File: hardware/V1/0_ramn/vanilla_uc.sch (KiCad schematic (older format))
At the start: 14 parts, among them J4 , U4 ATA6561-GAQW-N, U5 STM32L443CCTx, Y2 NX3225GD-8MHZ-STD-CRA-3

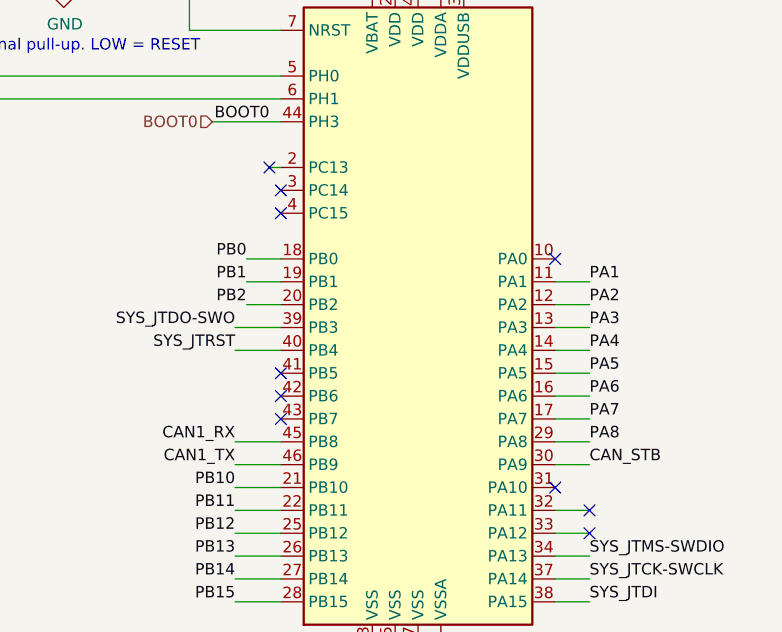
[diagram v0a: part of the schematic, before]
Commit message: Added initial V1 Firmware and Scripts
- Minor hardware fixes
- Minor documentation fixes
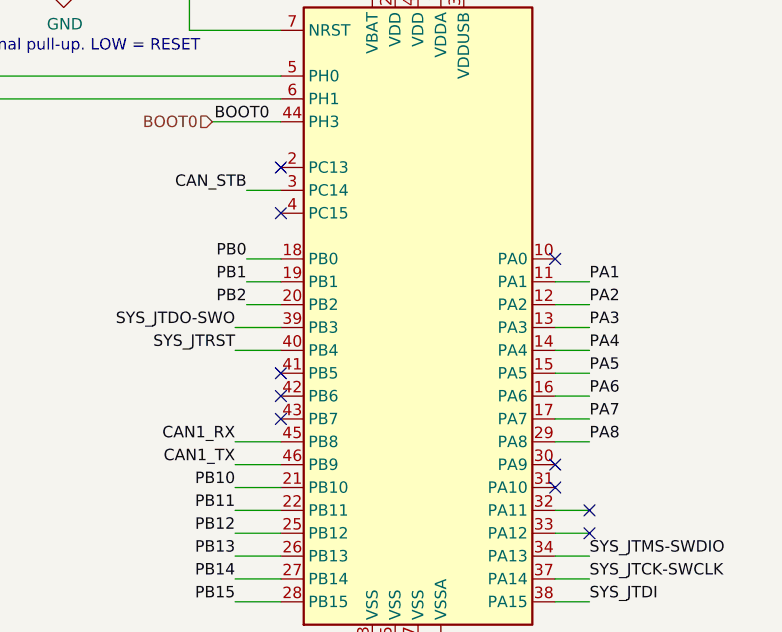
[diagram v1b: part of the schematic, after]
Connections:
- net CAN_STB: now also U5.3 (PC14); no longer U5.30 (PA9)
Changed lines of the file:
@@
 Sheet 4 9
 Title "RAMN: Resistant Automotive Miniature Network V1.0"
-Date "2021-02-20"
-Rev "A"
+Date "2021-06-01"
+Rev "B2L"
 Comp "Copyright (c) 2021 TOYOTA MOTOR CORPORATION. ALL RIGHTS RESERVED."
 Comment1 ""
@@
 BOOT0
 Wire Wire Line
-	8600 3550 8550 3550
-Text Label 9950 4850 0    50   ~ 0
-CAN_STB
-Wire Wire Line
 	8400 4750 8600 4750
 Text Label 8400 4750 2    50   ~ 0
@@
 Wire Wire Line
 	6550 3250 6550 3350
-NoConn ~ 8600 3650
 NoConn ~ 8600 3750
 $Sheet
@@
 Text Label 8200 2700 0    50   ~ 0
 nRST
-NoConn ~ 8550 3550
 NoConn ~ 9800 4950
 NoConn ~ 9800 3950
@@
 BOOT0
 Wire Wire Line
-	9950 4850 9800 4850
-Wire Wire Line
 	3050 3150 3050 3100
 Connection ~ 3050 3100
@@
 	1    0    0    -1
 $EndComp
+Text Label 8450 3650 2    50   ~ 0
+CAN_STB
+NoConn ~ 8600 3550
+Wire Wire Line
+	8600 3650 8450 3650
+NoConn ~ 9800 4850
 $EndSCHEMATC

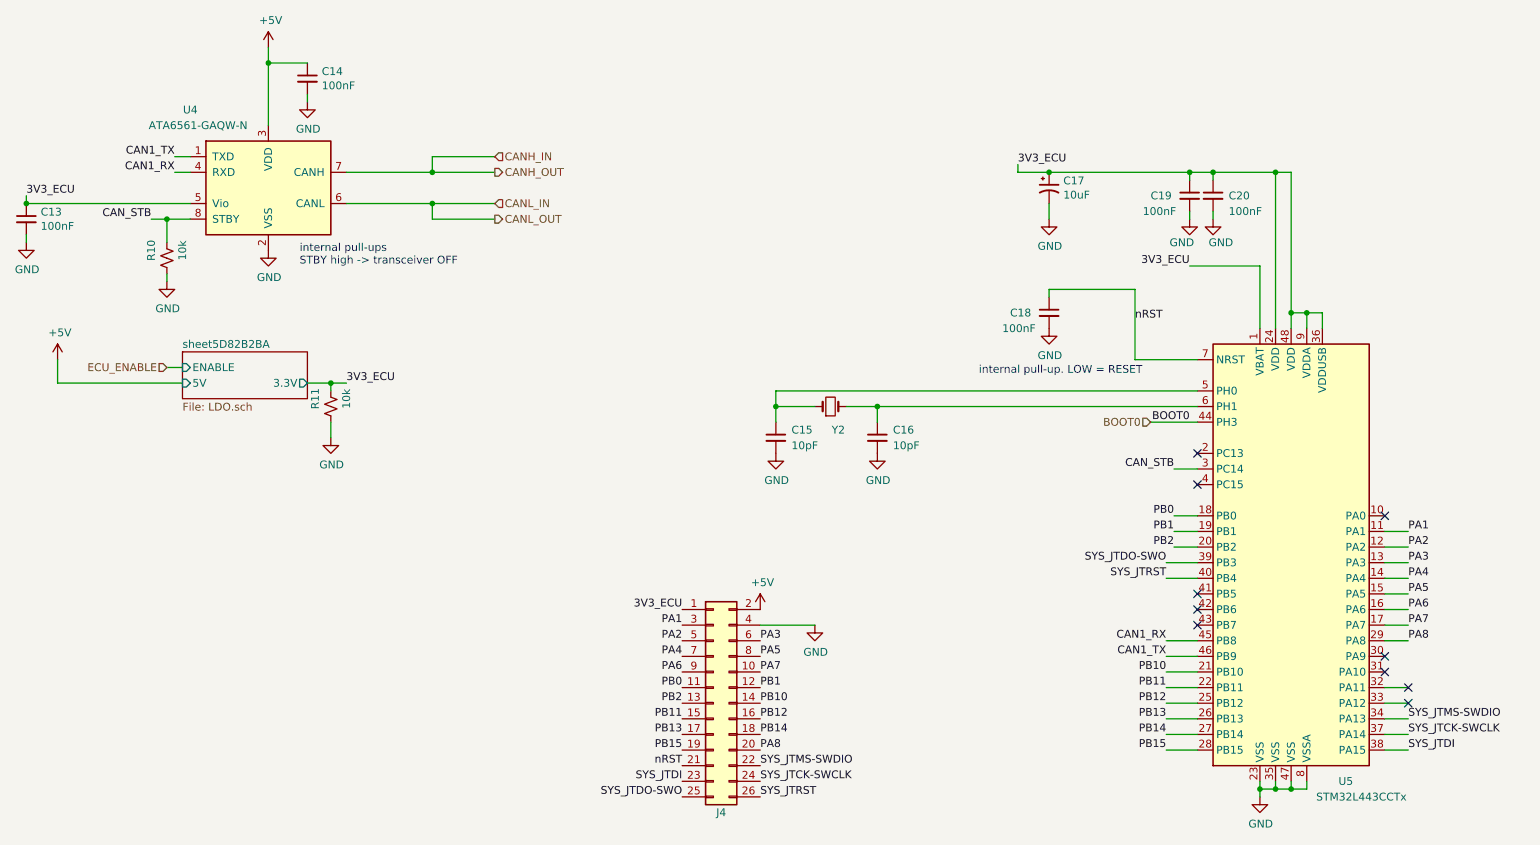
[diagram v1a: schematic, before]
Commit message: Updated schematics to show BOOT0 resistor settings for STM32L5 microcontrollers
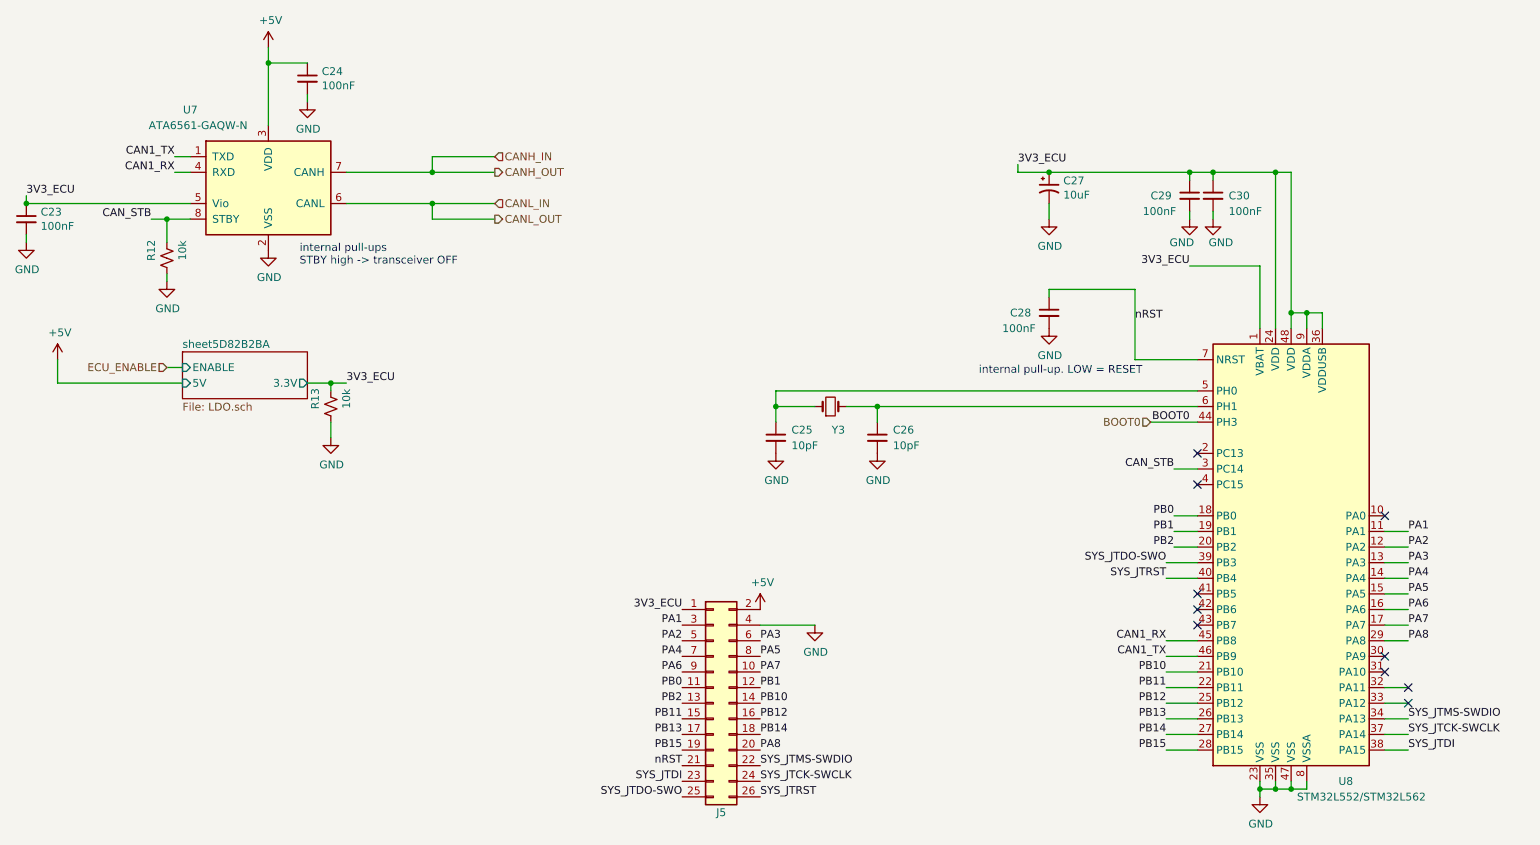
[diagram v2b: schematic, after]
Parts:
- U5: value STM32L443CCTx -> STM32L552/STM32L562
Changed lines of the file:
@@
 $Descr A4 11693 8268
 encoding utf-8
-Sheet 4 9
+Sheet 6 9
 Title "RAMN: Resistant Automotive Miniature Network V1.0"
-Date "2021-06-01"
+Date "2024-02-20"
 Rev "B2L"
-Comp "Copyright (c) 2021 TOYOTA MOTOR CORPORATION. ALL RIGHTS RESERVED."
+Comp "Copyright (c) 2024 TOYOTA MOTOR CORPORATION. ALL RIGHTS RESERVED."
 Comment1 ""
 Comment2 ""
@@
 AR Path="/5D815E09/5D82B2DA" Ref="#PWR028"  Part="1"
 AR Path="/5D8EDE42/5D82B2DA" Ref="#PWR047"  Part="1"
-F 0 "#PWR028" H 2650 2000 50  0001 C CNN
+F 0 "#PWR047" H 2650 2000 50  0001 C CNN
 F 1 "GND" H 2655 2077 50  0000 C CNN
 F 2 "" H 2650 2250 50  0001 C CNN
@@
 AR Path="/5D815E09/5D82B2F8" Ref="#PWR027"  Part="1"
 AR Path="/5D8EDE42/5D82B2F8" Ref="#PWR046"  Part="1"
-F 0 "#PWR027" H 2650 800 50  0001 C CNN
+F 0 "#PWR046" H 2650 800 50  0001 C CNN
 F 1 "+5V" H 2665 1123 50  0000 C CNN
 F 2 "" H 2650 950 50  0001 C CNN
@@
 AR Path="/5D815E09/5D82B303" Ref="#PWR029"  Part="1"
 AR Path="/5D8EDE42/5D82B303" Ref="#PWR048"  Part="1"
-F 0 "#PWR029" H 2900 1050 50  0001 C CNN
+F 0 "#PWR048" H 2900 1050 50  0001 C CNN
 F 1 "GND" H 2905 1127 50  0000 C CNN
 F 2 "" H 2900 1300 50  0001 C CNN
@@
 AR Path="/5D815E09/5D82B30A" Ref="C14"  Part="1"
 AR Path="/5D8EDE42/5D82B30A" Ref="C24"  Part="1"
-F 0 "C14" H 2992 1196 50  0000 L CNN
+F 0 "C24" H 2992 1196 50  0000 L CNN
 F 1 "100nF" H 2992 1105 50  0000 L CNN
 F 2 "Capacitor_SMD:C_0603_1608Metric" H 2900 1150 50  0001 C CNN
@@
 AR Path="/5D815E09/5D82B311" Ref="#PWR024"  Part="1"
 AR Path="/5D8EDE42/5D82B311" Ref="#PWR043"  Part="1"
-F 0 "#PWR024" H 1100 1950 50  0001 C CNN
+F 0 "#PWR043" H 1100 1950 50  0001 C CNN
 F 1 "GND" H 1105 2027 50  0000 C CNN
 F 2 "" H 1100 2200 50  0001 C CNN
@@
 AR Path="/5D815E09/5D82B318" Ref="C13"  Part="1"
 AR Path="/5D8EDE42/5D82B318" Ref="C23"  Part="1"
-F 0 "C13" H 1192 2096 50  0000 L CNN
+F 0 "C23" H 1192 2096 50  0000 L CNN
 F 1 "100nF" H 1192 2005 50  0000 L CNN
 F 2 "Capacitor_SMD:C_0603_1608Metric" H 1100 2050 50  0001 C CNN
@@
 AR Path="/5D815E09/5D82B31E" Ref="U4"  Part="1"
 AR Path="/5D8EDE42/5D82B31E" Ref="U7"  Part="1"
-F 0 "U4" H 2150 2350 50  0000 C CNN
+F 0 "U7" H 2150 2350 50  0000 C CNN
 F 1 "ATA6561-GAQW-N" H 2200 2250 50  0000 C CNN
 F 2 "Package_SO:SOIC-8_3.9x4.9mm_P1.27mm" H 2650 1350 50  0001 C CIN
@@
 AR Path="/5D815E09/5D82B368" Ref="#PWR032"  Part="1"
 AR Path="/5D8EDE42/5D82B368" Ref="#PWR051"  Part="1"
-F 0 "#PWR032" H 5900 3300 50  0001 C CNN
+F 0 "#PWR051" H 5900 3300 50  0001 C CNN
 F 1 "GND" H 5905 3377 50  0000 C CNN
 F 2 "" H 5900 3550 50  0001 C CNN
@@
 AR Path="/5D815E09/5D82B36E" Ref="#PWR034"  Part="1"
 AR Path="/5D8EDE42/5D82B36E" Ref="#PWR053"  Part="1"
-F 0 "#PWR034" H 6550 3300 50  0001 C CNN
+F 0 "#PWR053" H 6550 3300 50  0001 C CNN
 F 1 "GND" H 6555 3377 50  0000 C CNN
 F 2 "" H 6550 3550 50  0001 C CNN
@@
 AR Path="/5D815E09/5D82B376" Ref="C16"  Part="1"
 AR Path="/5D8EDE42/5D82B376" Ref="C26"  Part="1"
-F 0 "C16" H 6650 3500 50  0000 L CNN
+F 0 "C26" H 6650 3500 50  0000 L CNN
 F 1 "10pF" H 6650 3400 50  0000 L CNN
 F 2 "Capacitor_SMD:C_0603_1608Metric" H 6550 3450 50  0001 C CNN
@@
 AR Path="/5D815E09/5D82B37D" Ref="C15"  Part="1"
 AR Path="/5D8EDE42/5D82B37D" Ref="C25"  Part="1"
-F 0 "C15" H 6000 3500 50  0000 L CNN
+F 0 "C25" H 6000 3500 50  0000 L CNN
 F 1 "10pF" H 6000 3400 50  0000 L CNN
 F 2 "Capacitor_SMD:C_0603_1608Metric" H 5900 3450 50  0001 C CNN
@@
 AR Path="/5D815E09/5D82B383" Ref="Y2"  Part="1"
 AR Path="/5D8EDE42/5D82B383" Ref="Y3"  Part="1"
-F 0 "Y2" H 6300 3100 50  0000 C CNN
+F 0 "Y3" H 6300 3100 50  0000 C CNN
 F 1 "NX3225GD-8MHZ-STD-CRA-3" H 6500 3400 50  0001 C CNN
 F 2 "digikey-footprints:SMD-2_3.2x2.5mm" H 6250 3250 50  0001 C CNN
@@
 AR Path="/5D815E09/5D82B396" Ref="#PWR039"  Part="1"
 AR Path="/5D8EDE42/5D82B396" Ref="#PWR058"  Part="1"
-F 0 "#PWR039" H 9000 5500 50  0001 C CNN
+F 0 "#PWR058" H 9000 5500 50  0001 C CNN
 F 1 "GND" H 9005 5577 50  0000 C CNN
 F 2 "" H 9000 5750 50  0001 C CNN
@@
 AR Path="/5D815E09/5D82B3A9" Ref="#PWR036"  Part="1"
 AR Path="/5D8EDE42/5D82B3A9" Ref="#PWR055"  Part="1"
-F 0 "#PWR036" H 7650 2500 50  0001 C CNN
+F 0 "#PWR055" H 7650 2500 50  0001 C CNN
 F 1 "GND" H 7655 2577 50  0000 C CNN
 F 2 "" H 7650 2750 50  0001 C CNN
@@
 AR Path="/5D815E09/5D82B3B0" Ref="C18"  Part="1"
 AR Path="/5D8EDE42/5D82B3B0" Ref="C28"  Part="1"
-F 0 "C18" H 7400 2650 50  0000 L CNN
+F 0 "C28" H 7400 2650 50  0000 L CNN
 F 1 "100nF" H 7350 2550 50  0000 L CNN
 F 2 "Capacitor_SMD:C_0603_1608Metric" H 7650 2650 50  0001 C CNN
@@
 AR Path="/5D815E09/5D82B3B9" Ref="C17"  Part="1"
 AR Path="/5D8EDE42/5D82B3B9" Ref="C27"  Part="1"
-F 0 "C17" H 7741 1896 50  0000 L CNN
+F 0 "C27" H 7741 1896 50  0000 L CNN
 F 1 "10uF" H 7741 1805 50  0000 L CNN
 F 2 "Capacitor_SMD:C_1206_3216Metric" H 7650 1850 50  0001 C CNN
@@
 AR Path="/5D815E09/5D82B3C0" Ref="#PWR035"  Part="1"
 AR Path="/5D8EDE42/5D82B3C0" Ref="#PWR054"  Part="1"
-F 0 "#PWR035" H 7650 1800 50  0001 C CNN
+F 0 "#PWR054" H 7650 1800 50  0001 C CNN
 F 1 "GND" H 7655 1877 50  0000 C CNN
 F 2 "" H 7650 2050 50  0001 C CNN
@@
 AR Path="/5D815E09/5D82B3D2" Ref="#PWR037"  Part="1"
 AR Path="/5D8EDE42/5D82B3D2" Ref="#PWR056"  Part="1"
-F 0 "#PWR037" H 8550 1800 50  0001 C CNN
+F 0 "#PWR056" H 8550 1800 50  0001 C CNN
 F 1 "GND" H 8500 1900 50  0000 C CNN
 F 2 "" H 8550 2050 50  0001 C CNN
@@
 AR Path="/5D815E09/5D82B3D8" Ref="#PWR038"  Part="1"
 AR Path="/5D8EDE42/5D82B3D8" Ref="#PWR057"  Part="1"
-F 0 "#PWR038" H 8700 1800 50  0001 C CNN
+F 0 "#PWR057" H 8700 1800 50  0001 C CNN
 F 1 "GND" H 8750 1900 50  0000 C CNN
 F 2 "" H 8700 2050 50  0001 C CNN
@@
 AR Path="/5D815E09/5D82B3E8" Ref="C20"  Part="1"
 AR Path="/5D8EDE42/5D82B3E8" Ref="C30"  Part="1"
-F 0 "C20" H 8800 1900 50  0000 L CNN
+F 0 "C30" H 8800 1900 50  0000 L CNN
 F 1 "100nF" H 8800 1800 50  0000 L CNN
 F 2 "Capacitor_SMD:C_0603_1608Metric" H 8700 1900 50  0001 C CNN
@@
 AR Path="/5D815E09/5D82B3EF" Ref="C19"  Part="1"
 AR Path="/5D8EDE42/5D82B3EF" Ref="C29"  Part="1"
-F 0 "C19" H 8300 1900 50  0000 L CNN
+F 0 "C29" H 8300 1900 50  0000 L CNN
 F 1 "100nF" H 8250 1800 50  0000 L CNN
 F 2 "Capacitor_SMD:C_0603_1608Metric" H 8550 1900 50  0001 C CNN
@@
 AR Path="/5D815E09/5D82B3F5" Ref="U5"  Part="1"
 AR Path="/5D8EDE42/5D82B3F5" Ref="U8"  Part="1"
-F 0 "U5" H 9550 2650 50  0000 C CNN
-F 1 "STM32L443CCTx" H 9650 2550 50  0000 C CNN
+F 0 "U8" H 9550 2650 50  0000 C CNN
+F 1 "STM32L552/STM32L562" H 9650 2550 50  0000 C CNN
 F 2 "Package_QFP:LQFP-48_7x7mm_P0.5mm" H 8700 2750 50  0001 R CNN
 F 3 "http://www.st.com/st-web-ui/static/active/en/resource/technical/document/datasheet/DM00254865.pdf" H 9200 4150 50  0001 C CNN
@@
 AR Path="/5D815E09/5D82B410" Ref="#PWR025"  Part="1"
 AR Path="/5D8EDE42/5D82B410" Ref="#PWR044"  Part="1"
-F 0 "#PWR025" H 1300 2800 50  0001 C CNN
+F 0 "#PWR044" H 1300 2800 50  0001 C CNN
 F 1 "+5V" H 1315 3123 50  0000 C CNN
 F 2 "" H 1300 2950 50  0001 C CNN
@@
 AR Path="/5D815E09/5D881AE2" Ref="R10"  Part="1"
 AR Path="/5D8EDE42/5D881AE2" Ref="R12"  Part="1"
-F 0 "R10" V 1900 2350 50  0000 C CNN
+F 0 "R12" V 1900 2350 50  0000 C CNN
 F 1 "10k" V 2100 2350 50  0000 C CNN
 F 2 "Resistor_SMD:R_0603_1608Metric" H 2000 2300 50  0001 C CNN
@@
 AR Path="/5D815E09/5D88B634" Ref="#PWR026"  Part="1"
 AR Path="/5D8EDE42/5D88B634" Ref="#PWR045"  Part="1"
-F 0 "#PWR026" H 2000 2200 50  0001 C CNN
+F 0 "#PWR045" H 2000 2200 50  0001 C CNN
 F 1 "GND" H 2005 2277 50  0000 C CNN
 F 2 "" H 2000 2450 50  0001 C CNN
@@
 AR Path="/5D815E09/5DEDC6F4" Ref="#PWR033"  Part="1"
 AR Path="/5D8EDE42/5DEDC6F4" Ref="#PWR052"  Part="1"
-F 0 "#PWR033" H 6150 4400 50  0001 C CNN
+F 0 "#PWR052" H 6150 4400 50  0001 C CNN
 F 1 "GND" H 6155 4477 50  0000 C CNN
 F 2 "" H 6150 4650 50  0001 C CNN
@@
 AR Path="/5D8EDE42/5DEDC6FA" Ref="#PWR050"  Part="1"
 AR Path="/5D7DEA89/5DEDC6FA" Ref="#PWR?"  Part="1"
-F 0 "#PWR031" H 5800 4400 50  0001 C CNN
+F 0 "#PWR050" H 5800 4400 50  0001 C CNN
 F 1 "+5V" H 5815 4723 50  0000 C CNN
 F 2 "" H 5800 4550 50  0001 C CNN
@@
 AR Path="/5D815E09/5DEDC70D" Ref="J4"  Part="1"
 AR Path="/5D8EDE42/5DEDC70D" Ref="J5"  Part="1"
-F 0 "J4" H 5550 4450 50  0000 C CNN
+F 0 "J5" H 5550 4450 50  0000 C CNN
 F 1 " " H 5550 5876 50  0000 C CNN
 F 2 "Connector_PinSocket_2.54mm:PinSocket_2x13_P2.54mm_Vertical" H 5500 5150 50  0001 C CNN
@@
 AR Path="/5D815E09/5DF0F466" Ref="#PWR030"  Part="1"
 AR Path="/5D8EDE42/5DF0F466" Ref="#PWR049"  Part="1"
-F 0 "#PWR030" H 3050 3200 50  0001 C CNN
+F 0 "#PWR049" H 3050 3200 50  0001 C CNN
 F 1 "GND" H 3055 3277 50  0000 C CNN
 F 2 "" H 3050 3450 50  0001 C CNN
@@
 AR Path="/5D815E09/5DF090D2" Ref="R11"  Part="1"
 AR Path="/5D8EDE42/5DF090D2" Ref="R13"  Part="1"
-F 0 "R11" V 2950 3300 50  0000 C CNN
+F 0 "R13" V 2950 3300 50  0000 C CNN
 F 1 "10k" V 3150 3300 50  0000 C CNN
 F 2 "Resistor_SMD:R_0603_1608Metric" H 3050 3250 50  0001 C CNN
